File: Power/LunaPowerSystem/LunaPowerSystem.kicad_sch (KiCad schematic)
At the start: 13 parts, among them U1 Power Distribution Panel, U2 E-STOP, U3 Mini Power Distribution Panel, U4 Jetson Nano

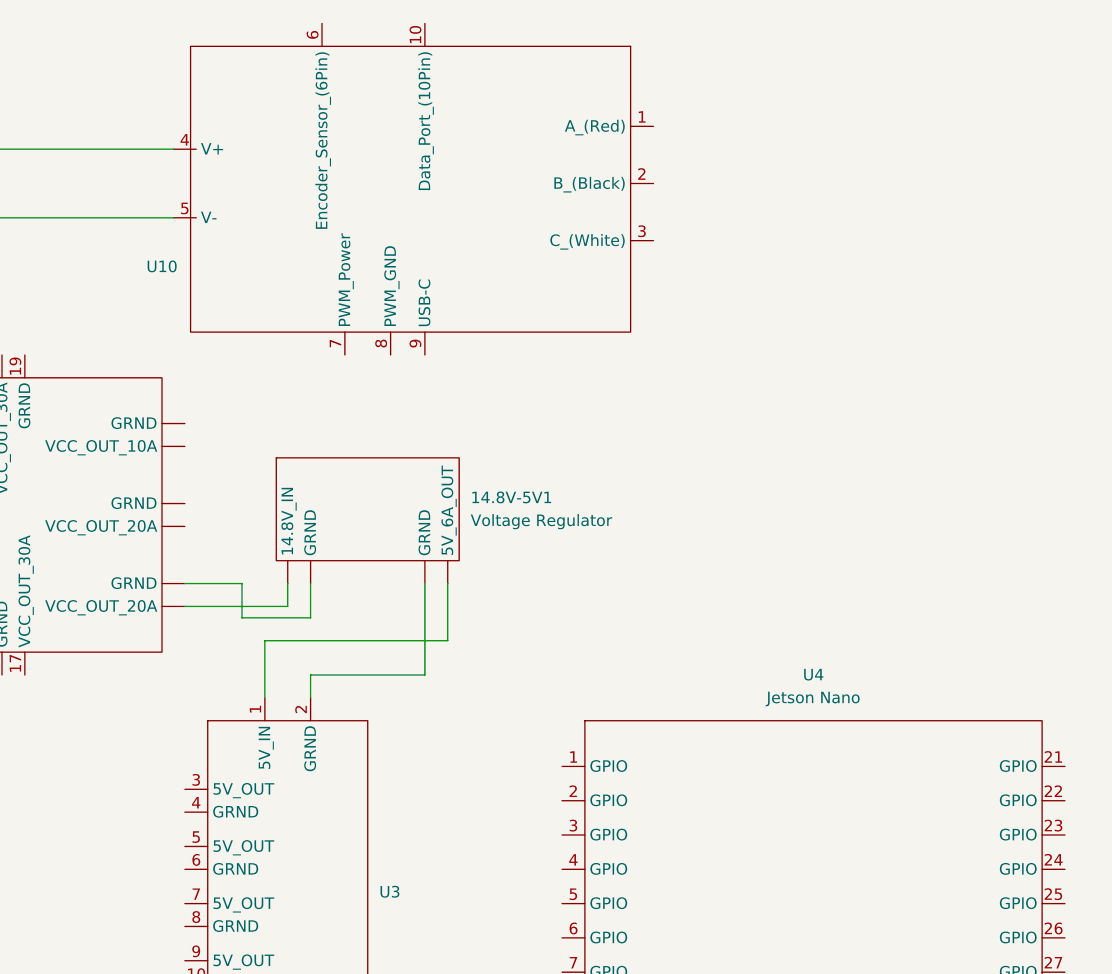
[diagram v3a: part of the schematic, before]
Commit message: Ported Linear Actuator to other schematics
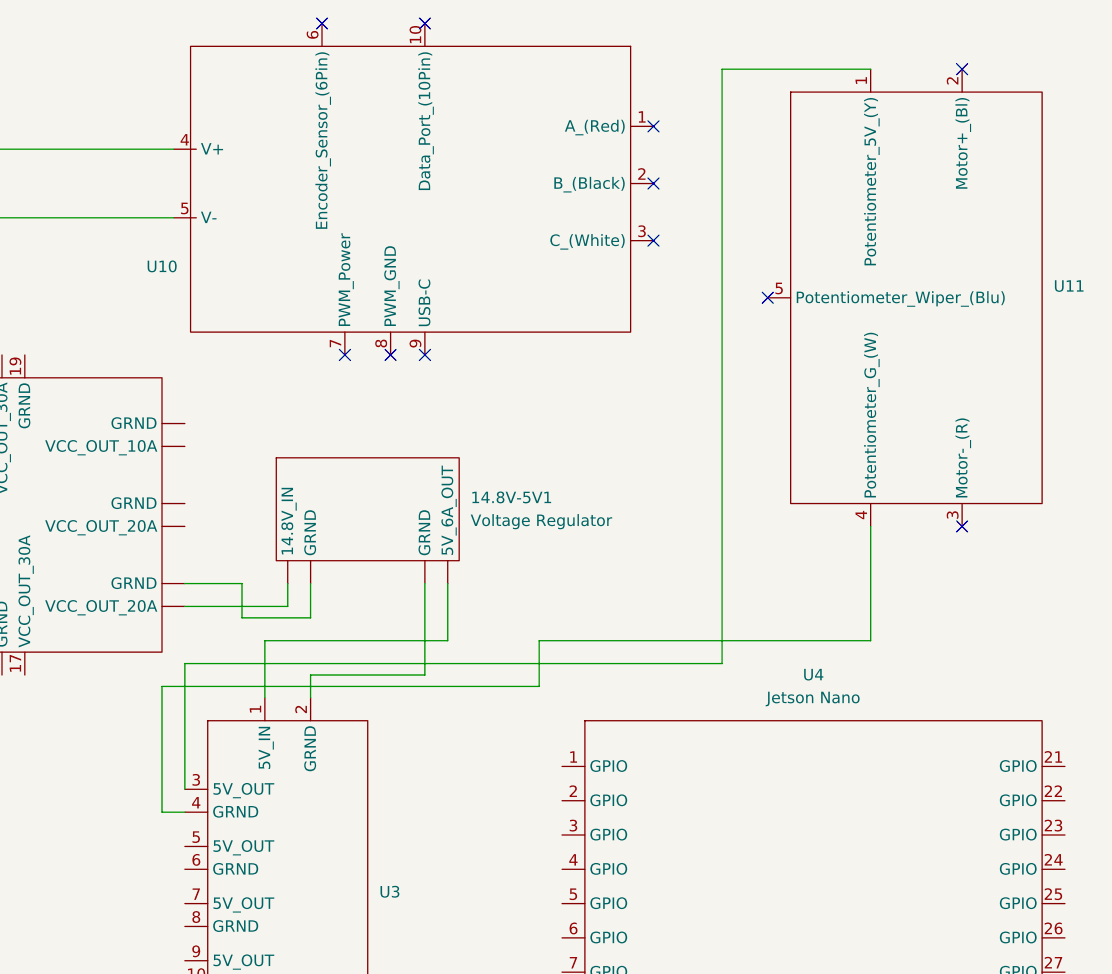
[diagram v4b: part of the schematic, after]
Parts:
- added U11: ~, symbol Lunabotics 2025-26:Feedback_Linear_Actuator
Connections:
- net at U1. (GRND): now also 14.8V-5V1. (5V_6A_OUT)
- net at 14.8V-5V1. (5V_6A_OUT): now also U3.2 (GRND); no longer U1. (GRND)
- net at U3.3 (5V_OUT): now also U11.1 (Potentiometer_5V_(Y))
- net at U3.4 (GRND): now also U11.4 (Potentiometer_G_(W))
- new net: 14.8V-5V1. (5V_6A_OUT), U1. (GRND)
- no-connect marks 1 -> 12
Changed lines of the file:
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@@
+	)
+	(no_connect
+		(at 320.04 20.32)
+	)
+	(no_connect
+		(at 248.92 15.24)
+	)
+	(no_connect
+		(at 251.46 52.07)
+	)
+	(no_connect
+		(at 285.75 26.67)
+	)
+	(no_connect
+		(at 260.35 15.24)
+	)
+	(no_connect
+		(at 260.35 52.07)
+	)
+	(no_connect
+		(at 298.45 45.72)
+	)
+	(no_connect
+		(at 320.04 71.12)
+	)
+	(no_connect
+		(at 285.75 33.02)
+	)
+	(no_connect
+		(at 285.75 39.37)
+	)
+	(no_connect
+		(at 256.54 52.07)
 	)
 	(no_connect
@@
 	(wire
 		(pts
+			(xy 231.14 102.87) (xy 233.68 102.87)
+		)
+		(stroke
+			(width 0)
+			(type default)
+			(color 0 0 0 1)
+		)
+	)
+	(wire
+		(pts
 			(xy 312.42 177.8) (xy 312.42 182.88)
 		)
@@
 	(wire
 		(pts
+			(xy 309.88 20.32) (xy 293.37 20.32)
+		)
+		(stroke
+			(width 0)
+			(type default)
+			(color 255 0 0 1)
+		)
+	)
+	(wire
+		(pts
+			(xy 273.05 88.9) (xy 231.14 88.9)
+		)
+		(stroke
+			(width 0)
+			(type default)
+			(color 0 0 0 1)
+		)
+	)
+	(wire
+		(pts
 			(xy 170.18 99.06) (xy 170.18 87.63)
 		)
@@
 	(wire
 		(pts
+			(xy 309.88 71.12) (xy 309.88 83.82)
+		)
+		(stroke
+			(width 0)
+			(type default)
+			(color 0 0 0 1)
+		)
+	)
+	(wire
+		(pts
 			(xy 120.65 120.65) (xy 120.65 100.33)
 		)
@@
 	(wire
 		(pts
+			(xy 293.37 86.36) (xy 233.68 86.36)
+		)
+		(stroke
+			(width 0)
+			(type default)
+			(color 255 0 0 1)
+		)
+	)
+	(wire
+		(pts
 			(xy 142.24 182.88) (xy 142.24 105.41)
 		)
@@
 	(wire
 		(pts
+			(xy 273.05 83.82) (xy 273.05 88.9)
+		)
+		(stroke
+			(width 0)
+			(type default)
+			(color 0 0 0 1)
+		)
+	)
+	(wire
+		(pts
 			(xy 229.87 125.73) (xy 229.87 182.88)
 		)
@@
 	(wire
 		(pts
+			(xy 231.14 88.9) (xy 231.14 102.87)
+		)
+		(stroke
+			(width 0)
+			(type default)
+			(color 0 0 0 1)
+		)
+	)
+	(wire
+		(pts
 			(xy 147.32 105.41) (xy 147.32 49.53)
 		)
@@
 	(wire
 		(pts
+			(xy 309.88 83.82) (xy 273.05 83.82)
+		)
+		(stroke
+			(width 0)
+			(type default)
+			(color 0 0 0 1)
+		)
+	)
+	(wire
+		(pts
 			(xy 135.89 182.88) (xy 142.24 182.88)
 		)
@@
 	(wire
 		(pts
+			(xy 233.68 86.36) (xy 233.68 100.33)
+		)
+		(stroke
+			(width 0)
+			(type default)
+			(color 255 0 0 1)
+		)
+	)
+	(wire
+		(pts
 			(xy 313.69 177.8) (xy 312.42 177.8)
 		)
@@
 			(type default)
 			(color 0 0 0 1)
+		)
+	)
+	(wire
+		(pts
+			(xy 293.37 20.32) (xy 293.37 86.36)
+		)
+		(stroke
+			(width 0)
+			(type default)
+			(color 255 0 0 1)
 		)
 	)
@@
 					(unit 1)
 				)
+			)
+		)
+	)
+	(symbol
+		(lib_id "Lunabotics 2025-26:Feedback_Linear_Actuator")
+		(at 314.96 45.72 0)
+		(unit 1)
+		(exclude_from_sim no)
+		(in_bom yes)
+		(on_board yes)
+		(dnp no)
+		(fields_autoplaced yes)
+		(property "Reference" "U11"
+			(at 330.2 44.4499 0)
+			(effects
+				(font
+					(size 1.27 1.27)
+				)
+				(justify left)
+			)
+		)
+		(property "Value" "~"
+			(at 330.2 46.9899 0)
+			(effects
+				(font
+					(size 1.27 1.27)
+				)
+				(justify left)
+			)
+		)
+		(property "Footprint" ""
+			(at 314.96 45.72 0)
+			(effects
+				(font
+					(size 1.27 1.27)
+				)
+				(hide yes)
+			)
+		)
+		(property "Datasheet" ""
+			(at 314.96 45.72 0)
+			(effects
+				(font
+					(size 1.27 1.27)
+				)
+				(hide yes)
+			)
+		)
+		(property "Description" ""
+			(at 314.96 45.72 0)
+			(effects
+				(font
+					(size 1.27 1.27)
+				)
+				(hide yes)
+			)
+		)
+		(pin "5"
+		)
+		(pin "3"
+		)
+		(pin "4"
+		)
+		(pin "1"
+		)
+		(pin "2"
+		)
+		(instances
+			(project ""
+				(path "/ddb47dc6-db2c-4ed2-99c0-9b98c5e956b4"
+					(reference "U11")
+					(unit 1)
+				)

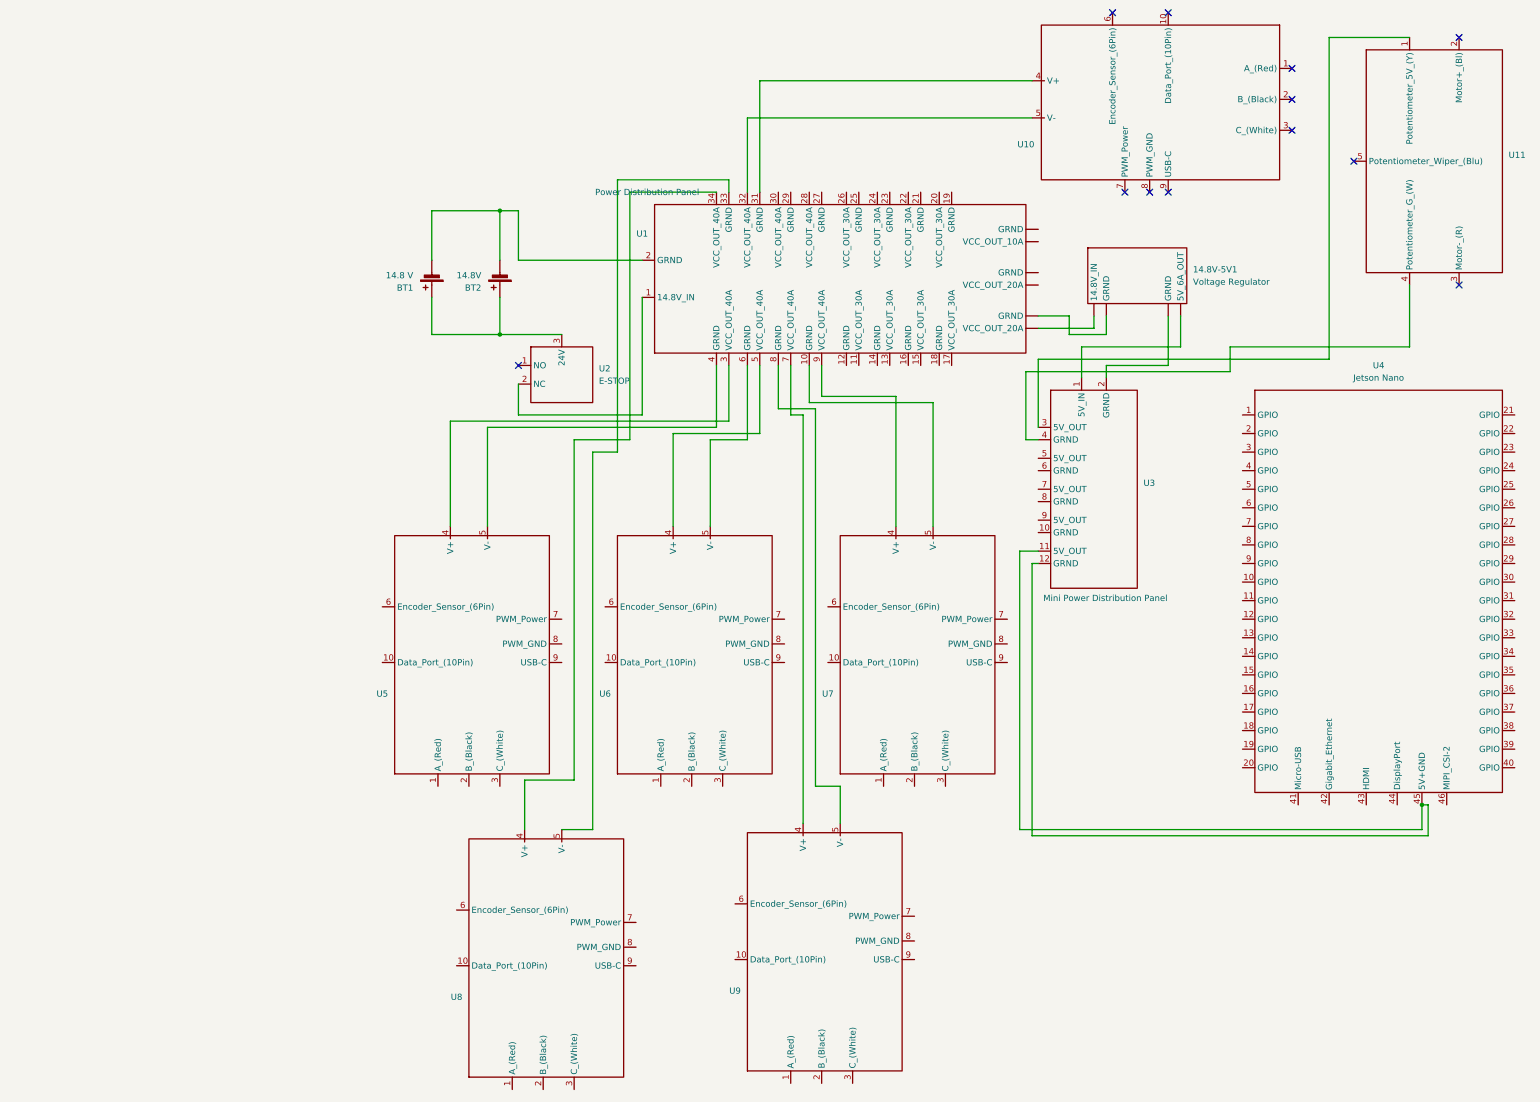
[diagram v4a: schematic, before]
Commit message: Finalized Schematics with linear actuator and updated encoder
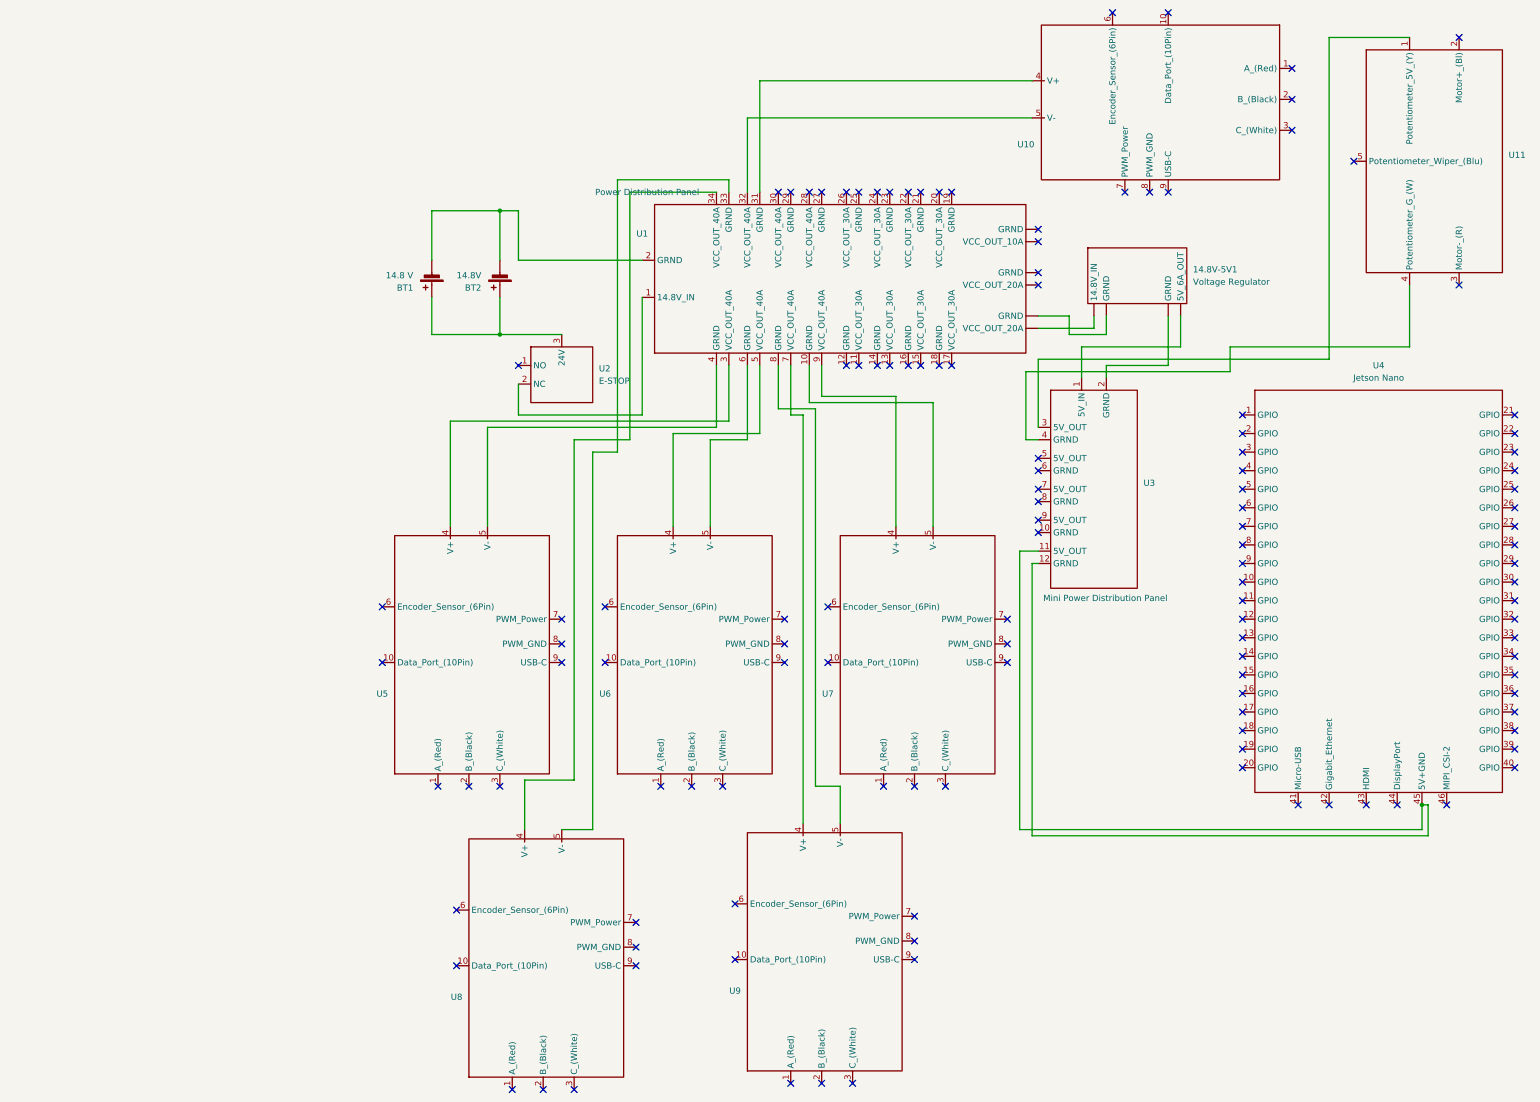
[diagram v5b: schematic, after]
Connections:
- net at U1. (GRND): now also 14.8V-5V1. (5V_6A_OUT)
- net at 14.8V-5V1. (5V_6A_OUT): now also U3.2 (GRND); no longer U1. (GRND)
- new net: 14.8V-5V1. (5V_6A_OUT), U1. (GRND)
- no-connect marks 12 -> 127

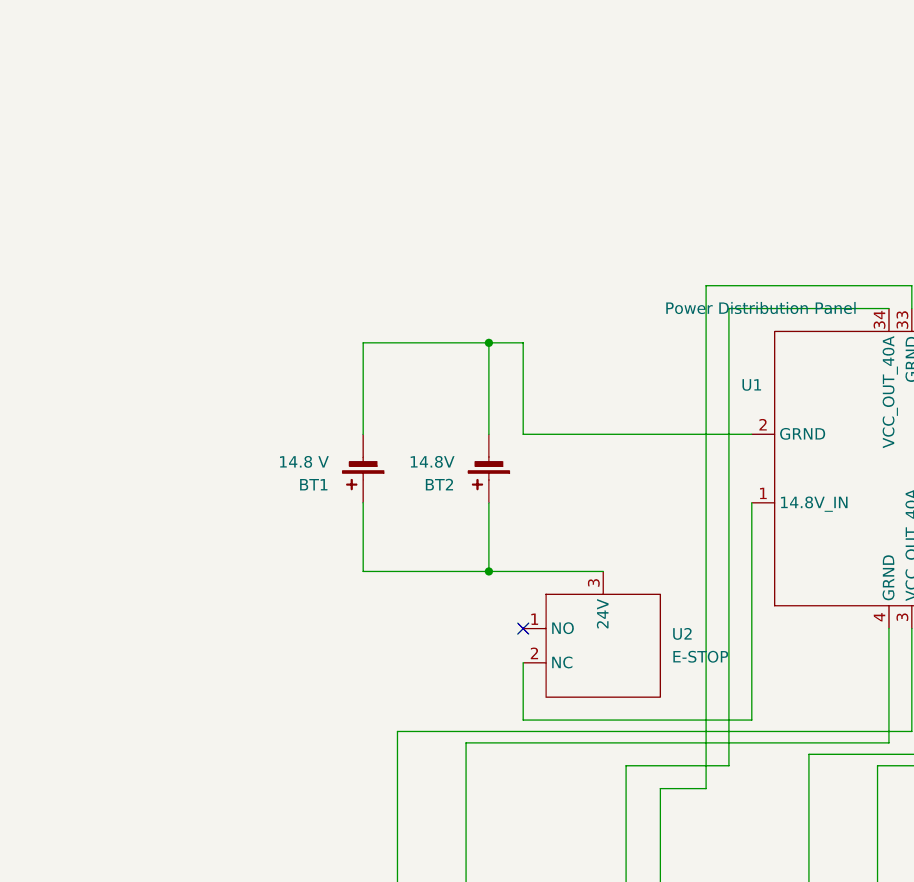
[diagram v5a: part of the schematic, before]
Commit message: Power System Changes
Added Power Meter and Power Meter Shunt to both power schematic and overall schematic
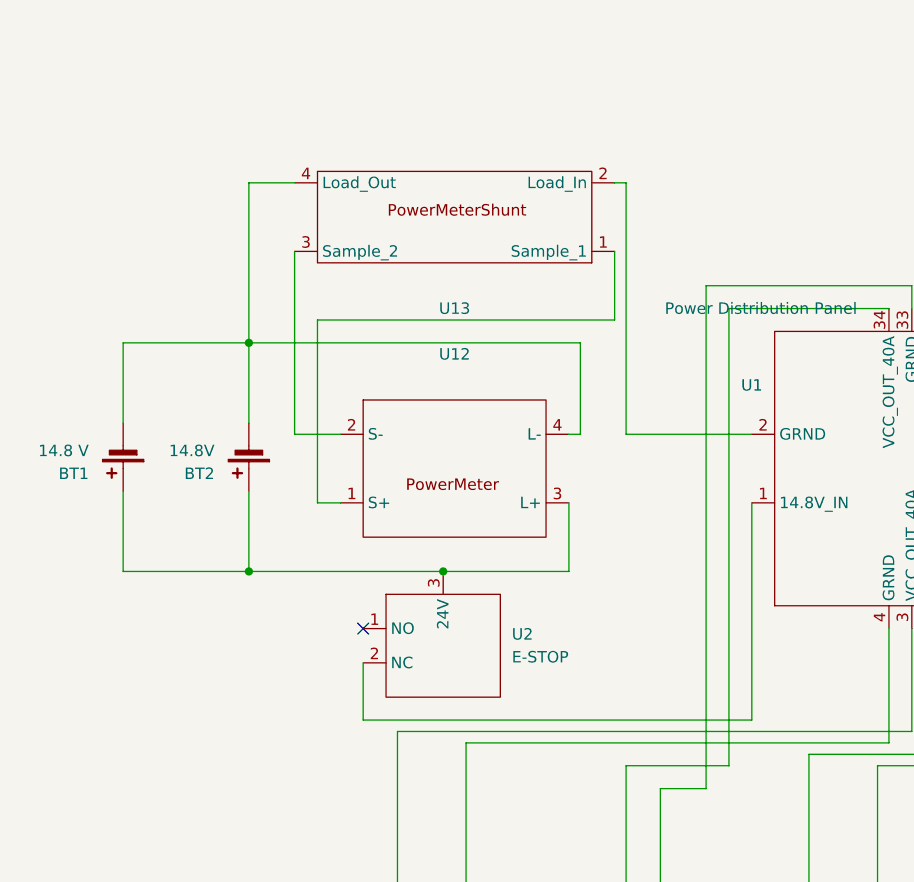
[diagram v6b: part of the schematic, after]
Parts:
- added U12: ~, symbol Lunabotics 2025-26:Power_Meter
- added U13: ~, symbol Lunabotics 2025-26:Power_Meter_Shunt
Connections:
- net at BT1.1 (+), BT2.1 (+), U2.3 (24V): now also U12.3 (L+)
- net at BT1.2 (-), BT2.2 (-): now also U12.4 (L-), U13.4 (Load_Out); no longer U1.2 (GRND)
- net at U1. (GRND): now also 14.8V-5V1. (5V_6A_OUT)
- net at 14.8V-5V1. (5V_6A_OUT): now also U3.2 (GRND); no longer U1. (GRND)
- new net: 14.8V-5V1. (5V_6A_OUT), U1. (GRND)
- new net: U1.2 (GRND), U13.2 (Load_In)
- new net: U12.1 (S+), U13.1 (Sample_1)
- new net: U12.2 (S-), U13.3 (Sample_2)
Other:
- moved on the sheet: BT1, BT2, U2
